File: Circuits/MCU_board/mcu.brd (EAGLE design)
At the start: 100 x 80 mm, 40 parts, among them IC1 RP111N331B-TR-FE, U1 TCA9548APWR, U2 USBLC6-2P6, U4 LSM9DS1, U5 STM32L452RECT6

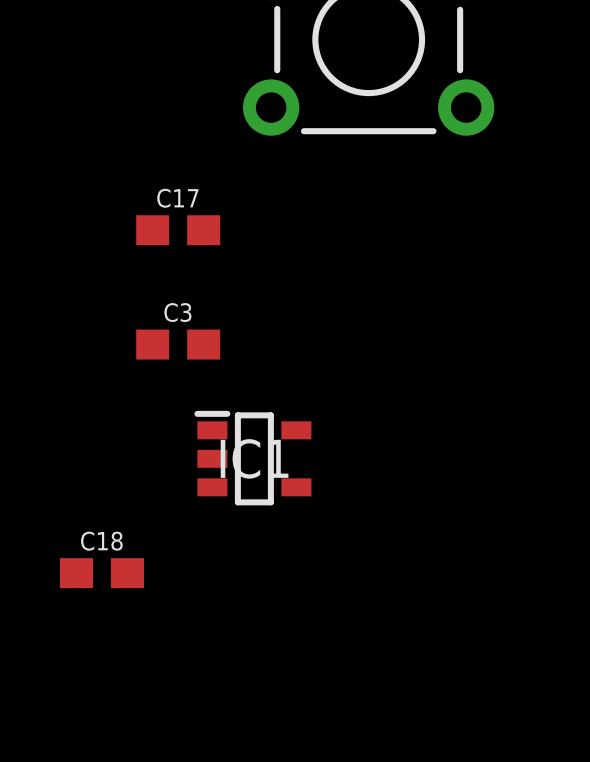
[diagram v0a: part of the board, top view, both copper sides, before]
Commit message: Changed all VCC to VDD, Fixed i2c bus issue for board IMU and baseboard IMU
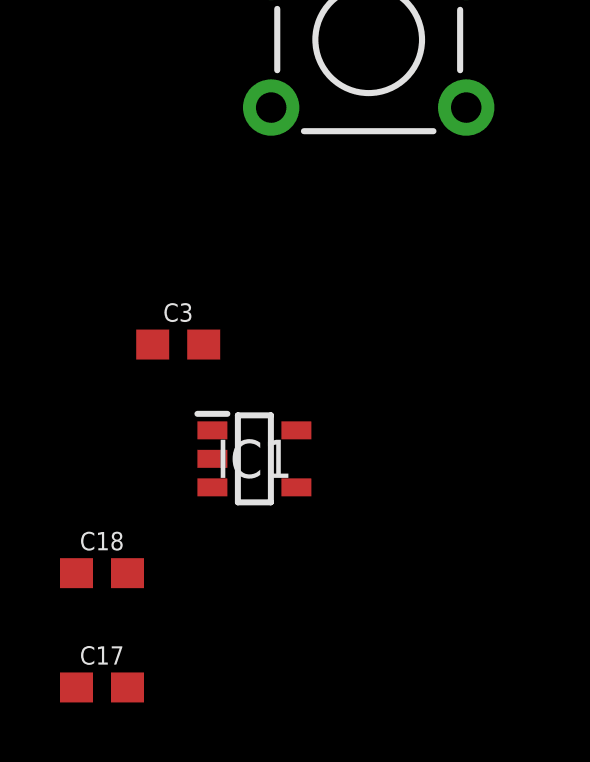
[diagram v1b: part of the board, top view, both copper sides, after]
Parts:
- C17: value 100nF -> 0.1uF
- moved C17 15.5 mm to (-50.8, -138.4)
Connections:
- removed net VCC: C2.1, C6.1, C8.1, R1.2, R2.2, R3.2, R4.2, R6.2, U4.1, U4.22, U4.23, U4.3
- net SCL5: no longer U$5.5
- net SCL6: no longer U4.2
- net SCL7: now also U$5.5, U4.2
- net SDA5: no longer U$5.6
- net SDA6: no longer U4.4
- net SDA7: now also U$5.6, U4.4
- net VDD: now also C2.1, C6.1, C8.1, R1.2, R2.2, R3.2, R4.2, R6.2, U4.1, U4.22, U4.23, U4.3
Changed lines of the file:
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@@
 <attribute name="VALUE" x="-41.91" y="-120.015" size="0.6096" layer="27" font="vector" ratio="20" align="top-center"/>
-</element>
-<element name="C17" library="SparkFun-Capacitors" package="0603" value="100nF" x="-48.26" y="-123.19" smashed="yes">
-<attribute name="NAME" x="-48.26" y="-122.428" size="0.6096" layer="25" font="vector" ratio="20" align="bottom-center"/>
-<attribute name="PROD_ID" value="CAP-12380" x="-48.26" y="-123.19" size="1.778" layer="27" display="off"/>
-<attribute name="VALUE" x="-48.26" y="-123.952" size="0.6096" layer="27" font="vector" ratio="20" align="top-center"/>
 </element>
 <element name="C3" library="SparkFun-Capacitors" package="0603" value="1 uF" x="-48.26" y="-127" smashed="yes">
@@
 <attribute name="VALUE" x="-50.8" y="-135.382" size="0.6096" layer="27" font="vector" ratio="20" align="top-center"/>
 </element>
+<element name="C17" library="SparkFun-Capacitors" package="0603" value="0.1uF" x="-50.8" y="-138.43" smashed="yes">
+<attribute name="NAME" x="-50.8" y="-137.668" size="0.6096" layer="25" font="vector" ratio="20" align="bottom-center"/>
+<attribute name="PROD_ID" value="CAP-00810" x="-50.8" y="-138.43" size="1.778" layer="27" display="off"/>
+<attribute name="VALUE" x="-50.8" y="-139.192" size="0.6096" layer="27" font="vector" ratio="20" align="top-center"/>
+</element>
 </elements>
 <signals>
 <signal name="VBAT">
 <contactref element="U5" pad="1"/>
-</signal>
-<signal name="VCC">
-<contactref element="U4" pad="23"/>
-<contactref element="U4" pad="22"/>
-<contactref element="C6" pad="1"/>
-<contactref element="C8" pad="1"/>
-<contactref element="U4" pad="1"/>
-<contactref element="U4" pad="3"/>
-<contactref element="C2" pad="1"/>
-<contactref element="R4" pad="2"/>
-<contactref element="R3" pad="2"/>
-<contactref element="R2" pad="2"/>
-<contactref element="R1" pad="2"/>
-<contactref element="R6" pad="2"/>
-<wire x1="-43.6" y1="-16.51" x2="-43.6" y2="-110.49" width="0" layer="19" extent="1-1"/>
-<wire x1="-43.6" y1="-12.7" x2="-43.6" y2="-16.51" width="0" layer="19" extent="1-1"/>
-<wire x1="-39.79" y1="-12.7" x2="-43.6" y2="-12.7" width="0" layer="19" extent="1-1"/>
-<wire x1="-35.98" y1="-12.7" x2="-39.79" y2="-12.7" width="0" layer="19" extent="1-1"/>
-<wire x1="-45.3" y1="-8.89" x2="-43.6" y2="-12.7" width="0" layer="19" extent="1-1"/>
-<wire x1="-37.68" y1="-8.89" x2="-35.98" y2="-12.7" width="0" layer="19" extent="1-1"/>
-<wire x1="-45.925" y1="-3.595" x2="-45.3" y2="-8.89" width="0" layer="19" extent="1-1"/>
-<wire x1="-45.955" y1="-2.585" x2="-45.925" y2="-3.595" width="0" layer="19" extent="1-1"/>
-<wire x1="-45.095" y1="-2.585" x2="-45.955" y2="-2.585" width="0" layer="19" extent="1-1"/>
-<wire x1="-44.665" y1="-2.585" x2="-45.095" y2="-2.585" width="0" layer="19" extent="1-1"/>
-<wire x1="-37.68" y1="-2.54" x2="-37.68" y2="-8.89" width="0" layer="19" extent="1-1"/>
 </signal>
 <signal name="GND">
@@
 <contactref element="R5" pad="1"/>
 <contactref element="S1" pad="1"/>
-<contactref element="C17" pad="2"/>
 <contactref element="C3" pad="2"/>
 <contactref element="C5" pad="2"/>
@@
 <contactref element="U2" pad="2"/>
 <contactref element="C18" pad="2"/>
+<contactref element="C17" pad="2"/>
+<wire x1="-49.95" y1="-134.62" x2="-49.95" y2="-138.43" width="0" layer="19" extent="1-1"/>
 <wire x1="-47.12" y1="-130.81" x2="-49.95" y2="-134.62" width="0" layer="19" extent="1-1"/>
 <wire x1="-47.41" y1="-127" x2="-47.12" y2="-130.81" width="0" layer="19" extent="1-1"/>
-<wire x1="-47.41" y1="-123.19" x2="-47.41" y2="-127" width="0" layer="19" extent="1-1"/>
-<wire x1="-45.1612" y1="-114.5794" x2="-47.41" y2="-123.19" width="0" layer="19" extent="1-1"/>
+<wire x1="-45.1612" y1="-114.5794" x2="-47.41" y2="-127" width="0" layer="19" extent="1-1"/>
 <wire x1="-45.3" y1="-106.68" x2="-45.1612" y2="-114.5794" width="0" layer="19" extent="1-1"/>
 <wire x1="-44.45" y1="-102.87" x2="-45.3" y2="-106.68" width="0" layer="19" extent="1-1"/>
@@
 <contactref element="IC1" pad="5"/>
 <contactref element="IC1" pad="4"/>
+<contactref element="R6" pad="2"/>
+<contactref element="U4" pad="23"/>
+<contactref element="U4" pad="22"/>
+<contactref element="C6" pad="1"/>
+<contactref element="C8" pad="1"/>
+<contactref element="U4" pad="1"/>
+<contactref element="U4" pad="3"/>
+<contactref element="C2" pad="1"/>
+<contactref element="R1" pad="2"/>
+<contactref element="R2" pad="2"/>
+<contactref element="R3" pad="2"/>
+<contactref element="R4" pad="2"/>
 <wire x1="-44.32" y1="-129.86" x2="-49.11" y2="-127" width="0" layer="19" extent="1-1"/>
 <wire x1="-44.32" y1="-131.76" x2="-44.32" y2="-129.86" width="0" layer="19" extent="1-1"/>
-<wire x1="-44.45" y1="-97.79" x2="-49.11" y2="-127" width="0" layer="19" extent="1-1"/>
+<wire x1="-43.6" y1="-110.49" x2="-49.11" y2="-127" width="0" layer="19" extent="1-1"/>
+<wire x1="-44.45" y1="-97.79" x2="-43.6" y2="-110.49" width="0" layer="19" extent="1-1"/>
 <wire x1="-38.91" y1="-80.08" x2="-44.45" y2="-97.79" width="0" layer="19" extent="1-1"/>
 <wire x1="-38.91" y1="-71.19" x2="-38.91" y2="-80.08" width="0" layer="19" extent="1-1"/>
@@
 <wire x1="-45.3" y1="-24.13" x2="-45.3" y2="-27.94" width="0" layer="19" extent="1-1"/>
 <wire x1="-45.3" y1="-20.32" x2="-45.3" y2="-24.13" width="0" layer="19" extent="1-1"/>
-<wire x1="-23.07" y1="1.87" x2="-45.3" y2="-20.32" width="0" layer="19" extent="1-1"/>
+<wire x1="-43.6" y1="-16.51" x2="-45.3" y2="-20.32" width="0" layer="19" extent="1-1"/>
+<wire x1="-43.6" y1="-12.7" x2="-43.6" y2="-16.51" width="0" layer="19" extent="1-1"/>
+<wire x1="-39.79" y1="-12.7" x2="-43.6" y2="-12.7" width="0" layer="19" extent="1-1"/>
+<wire x1="-35.98" y1="-12.7" x2="-39.79" y2="-12.7" width="0" layer="19" extent="1-1"/>
+<wire x1="-45.3" y1="-8.89" x2="-43.6" y2="-12.7" width="0" layer="19" extent="1-1"/>
+<wire x1="-37.68" y1="-8.89" x2="-35.98" y2="-12.7" width="0" layer="19" extent="1-1"/>
+<wire x1="-45.925" y1="-3.595" x2="-45.3" y2="-8.89" width="0" layer="19" extent="1-1"/>
+<wire x1="-45.955" y1="-2.585" x2="-45.925" y2="-3.595" width="0" layer="19" extent="1-1"/>
+<wire x1="-45.095" y1="-2.585" x2="-45.955" y2="-2.585" width="0" layer="19" extent="1-1"/>
+<wire x1="-44.665" y1="-2.585" x2="-45.095" y2="-2.585" width="0" layer="19" extent="1-1"/>
+<wire x1="-37.68" y1="-2.54" x2="-37.68" y2="-8.89" width="0" layer="19" extent="1-1"/>
+<wire x1="-23.07" y1="1.87" x2="-37.68" y2="-2.54" width="0" layer="19" extent="1-1"/>
 <wire x1="-16.57" y1="1.87" x2="-23.07" y2="1.87" width="0" layer="19" extent="1-1"/>
 <wire x1="-14.57" y1="11.37" x2="-16.57" y2="1.87" width="0" layer="19" extent="1-1"/>
@@
 <signal name="SCL7">
 <contactref element="U1" pad="20"/>
+<contactref element="U$5" pad="5"/>
+<contactref element="U4" pad="2"/>
+<wire x1="-45.925" y1="-3.165" x2="-37.91" y2="-80.08" width="0" layer="19" extent="1-1"/>
+<wire x1="34.585" y1="57.5278" x2="-45.925" y2="-3.165" width="0" layer="19" extent="1-1"/>
 </signal>
 <signal name="SDA7">
 <contactref element="U1" pad="19"/>
+<contactref element="U$5" pad="6"/>
+<contactref element="U4" pad="4"/>
+<wire x1="-45.925" y1="-4.025" x2="-36.91" y2="-80.08" width="0" layer="19" extent="1-1"/>
+<wire x1="35.235" y1="57.5278" x2="-45.925" y2="-4.025" width="0" layer="19" extent="1-1"/>
 </signal>
 <signal name="SCL6">
 <contactref element="U1" pad="18"/>
 <contactref element="U$5" pad="1"/>
-<contactref element="U4" pad="2"/>
-<wire x1="-45.925" y1="-3.165" x2="-41.91" y2="-80.08" width="0" layer="19" extent="1-1"/>
-<wire x1="35.885" y1="57.5278" x2="-45.925" y2="-3.165" width="0" layer="19" extent="1-1"/>
+<wire x1="35.885" y1="57.5278" x2="-41.91" y2="-80.08" width="0" layer="19" extent="1-1"/>
 </signal>
 <signal name="SDA6">
 <contactref element="U1" pad="17"/>
 <contactref element="U$5" pad="2"/>
-<contactref element="U4" pad="4"/>
-<wire x1="-45.925" y1="-4.025" x2="-40.91" y2="-80.08" width="0" layer="19" extent="1-1"/>
-<wire x1="36.535" y1="57.5278" x2="-45.925" y2="-4.025" width="0" layer="19" extent="1-1"/>
+<wire x1="36.535" y1="57.5278" x2="-40.91" y2="-80.08" width="0" layer="19" extent="1-1"/>
 </signal>
 <signal name="SCL5">
 <contactref element="U1" pad="16"/>
 <contactref element="U$4" pad="1"/>
-<contactref element="U$5" pad="5"/>
-<wire x1="-41.91" y1="-71.19" x2="-37.91" y2="-80.08" width="0" layer="19" extent="1-1"/>
 <wire x1="37.185" y1="57.5278" x2="-41.91" y2="-71.19" width="0" layer="19" extent="1-1"/>
 </signal>
@@
 <contactref element="U1" pad="15"/>
 <contactref element="U$4" pad="2"/>
-<contactref element="U$5" pad="6"/>
-<wire x1="-40.91" y1="-71.19" x2="-36.91" y2="-80.08" width="0" layer="19" extent="1-1"/>
 <wire x1="37.835" y1="57.5278" x2="-40.91" y2="-71.19" width="0" layer="19" extent="1-1"/>
 </signal>
@@
 <signal name="N$4">
 <contactref element="S1" pad="3"/>
+<contactref element="U5" pad="7"/>
 <contactref element="C17" pad="1"/>
-<contactref element="U5" pad="7"/>
-<wire x1="-45.1612" y1="-119.1006" x2="-49.11" y2="-123.19" width="0" layer="19" extent="1-1"/>
+<wire x1="-45.1612" y1="-119.1006" x2="-51.65" y2="-138.43" width="0" layer="19" extent="1-1"/>
 <wire x1="-26.07" y1="8.37" x2="-45.1612" y2="-119.1006" width="0" layer="19" extent="1-1"/>
 </signal>

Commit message: Added i2c resistors - pulled high, Fixed capacitor package size, moved schematics around to be more organized
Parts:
- added R10, R11, R12, R13, R14, R15, R16, R17, R18, R19, R20, R7, R8, R9: 4.7k, SparkFun-Resistors:0603
- C11, C13, C15, C9: value 100nF -> 0.1uF
- C3: value 1 uF -> 1.0uF
- C5: device SparkFun-Capacitors:0402 -> SparkFun-Capacitors:0603
- R1, R3: value 10k -> 4.7k
- moved C5 320.2 mm to (-50.8, -276.9)
- moved C10 283.3 mm to (-50.8, -307.3)
- moved C12 279.5 mm to (-50.8, -311.1)
- moved C14 275.7 mm to (-50.8, -315.0)
- moved C9 271.9 mm to (-50.8, -292.1)
- moved C16 271.9 mm to (-50.8, -318.8)
- moved C11 268.0 mm to (-50.8, -295.9)
- moved C13 264.2 mm to (-50.8, -299.7)
- moved C15 260.4 mm to (-50.8, -303.5)
- moved R3 192.3 mm to (-50.8, -204.5)
- moved R1 188.1 mm to (-50.8, -200.7)
- moved R4 161.0 mm to (-0.85, -171.4)
- moved C3 153.7 mm to (-50.8, -280.7)
- moved R2 151.4 mm to (-0.85, -158.8)
- moved C17 123.2 mm to (-50.8, -261.6)
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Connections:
- removed net SA0: R1.1, U4.5
- removed net SA1: R3.1, U4.6
- new net N$3: C17.1
- net GND: now also U4.5, U4.6
- net N$4: no longer C17.1
- net SCL0: now also R3.1
- net SCL1: now also R8.1
- net SCL2: now also R10.1
- net SCL3: now also R12.1
- net SCL4: now also R14.1
- net SCL5: now also R16.1
- net SCL6: now also R18.1
- net SCL7: now also R20.1
- net SDA0: now also R1.1
- net SDA1: now also R7.1
- net SDA2: now also R9.1
- net SDA3: now also R11.1
- net SDA4: now also R13.1
- net SDA5: now also R15.1
- net SDA6: now also R17.1
- net SDA7: now also R19.1
- net VDD: now also R10.2, R11.2, R12.2, R13.2, R14.2, R15.2, R16.2, R17.2, R18.2, R19.2, R20.2, R7.2, R8.2, R9.2

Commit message: Add FTDI chip to MCU board
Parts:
- added C19: 4.7uF, SparkFun-Capacitors:0603
- added C20, C21: 0.1uF, SparkFun-Capacitors:0603
- added C22: 10nF, SparkFun-Capacitors:0603
- added C23, C24: 47pF, SparkFun-Capacitors:0603
- added IC2: FT230XS, ftdichip:SSOP16
- added MI0603K300R-10: 30Ω/1.8A, SparkFun-Coils:0603
- added R21, R22, R27, R28: 4.7k, SparkFun-Resistors:0603
- added R23, R24, R25, R26: 10k, SparkFun-Resistors:0603
- added RX_LED, TX_LED: GREEN, SparkFun-LED:LED-0603
- moved R20 398.1 mm to (-0.85, -652.8)
- moved R19 389.3 mm to (-0.85, -640.1)
- moved R18 380.5 mm to (-0.85, -627.4)
- moved R17 371.7 mm to (-0.85, -614.7)
- moved R16 362.9 mm to (-0.85, -602.0)
- moved R15 354.1 mm to (-0.85, -589.3)
- moved R14 345.3 mm to (-0.85, -576.6)
- moved R13 336.5 mm to (-0.85, -563.9)
- moved R12 327.7 mm to (-0.85, -551.2)
- moved R11 318.9 mm to (-0.85, -538.5)
- moved R10 310.1 mm to (-0.85, -525.8)
- moved R9 301.3 mm to (-0.85, -513.1)
- moved R8 292.6 mm to (-0.85, -500.4)
- moved R7 283.8 mm to (-0.85, -487.7)
- moved R3 275.1 mm to (-0.85, -475.0)
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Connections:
- net N$4 renamed NRST
- new net CTS: IC2.6, R25.1, U5.14
- new net N$10: R28.2, RX_LED.A
- new net N$11: IC2.7, RX_LED.C
- new net N$6: IC2.9, R21.2
- new net N$7: IC2.8, R22.1
- new net N$8: R27.2, TX_LED.A
- new net N$9: IC2.14, TX_LED.C
- new net RTS: IC2.2, R26.1, U5.15
- new net RXD: IC2.4, R24.1, U5.17
- new net TXD: IC2.1, R23.1, U5.16
- new net VCCIO: C20.1, IC2.10, IC2.11, IC2.3, R23.2, R24.2, R25.2, R26.2
- new net VCC_USB: C19.1, C21.1, IC2.12, MI0603K300R-10.1
- net GND: now also C19.2, C20.2, C21.2, C22.2, C23.2, C24.2, IC2.13, IC2.5
- net USB_D+: now also C24.1, R22.2
- net USB_D-: now also C23.1, R21.1
- net VBUS: now also C22.1, MI0603K300R-10.2
- net VDD: now also R27.1, R28.1

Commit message: Fix resistors in FTDI
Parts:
- R21, R22: value 4.7k -> 27R
- R27, R28: value 4.7k -> 270R
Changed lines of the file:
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@@
 <attribute name="VALUE" x="-50.8" y="-334.772" size="0.6096" layer="27" font="vector" ratio="20" align="top-center"/>
 </element>
-<element name="R21" library="SparkFun-Resistors" package="0603" value="4.7k" x="-0.85" y="-665.48" smashed="yes">
+<element name="R21" library="SparkFun-Resistors" package="0603" value="27R" x="-0.85" y="-665.48" smashed="yes">
 <attribute name="NAME" x="-0.85" y="-664.718" size="0.6096" layer="25" font="vector" ratio="20" align="bottom-center"/>
 <attribute name="PROD_ID" value="RES-07857" x="-0.85" y="-665.48" size="1.778" layer="27" display="off"/>
 <attribute name="VALUE" x="-0.85" y="-666.242" size="0.6096" layer="27" font="vector" ratio="20" align="top-center"/>
 </element>
-<element name="R22" library="SparkFun-Resistors" package="0603" value="4.7k" x="-0.85" y="-678.18" smashed="yes">
+<element name="R22" library="SparkFun-Resistors" package="0603" value="27R" x="-0.85" y="-678.18" smashed="yes">
 <attribute name="NAME" x="-0.85" y="-677.418" size="0.6096" layer="25" font="vector" ratio="20" align="bottom-center"/>
 <attribute name="PROD_ID" value="RES-07857" x="-0.85" y="-678.18" size="1.778" layer="27" display="off"/>
@@
 <attribute name="VALUE" x="-52.07" y="-365.252" size="0.6096" layer="27" font="vector" ratio="20" align="top-center"/>
 </element>
-<element name="R27" library="SparkFun-Resistors" package="0603" value="4.7k" x="-0.85" y="-690.88" smashed="yes">
+<element name="R27" library="SparkFun-Resistors" package="0603" value="270R" x="-0.85" y="-690.88" smashed="yes">
 <attribute name="NAME" x="-0.85" y="-690.118" size="0.6096" layer="25" font="vector" ratio="20" align="bottom-center"/>
 <attribute name="PROD_ID" value="RES-07857" x="-0.85" y="-690.88" size="1.778" layer="27" display="off"/>
@@
 <attribute name="VALUE" x="-52.07" y="-399.415" size="0.6096" layer="27" font="vector" ratio="20" align="top-center"/>
 </element>
-<element name="R28" library="SparkFun-Resistors" package="0603" value="4.7k" x="-0.85" y="-703.58" smashed="yes">
+<element name="R28" library="SparkFun-Resistors" package="0603" value="270R" x="-0.85" y="-703.58" smashed="yes">
 <attribute name="NAME" x="-0.85" y="-702.818" size="0.6096" layer="25" font="vector" ratio="20" align="bottom-center"/>
 <attribute name="PROD_ID" value="RES-07857" x="-0.85" y="-707.39" size="1.778" layer="27" display="off"/>

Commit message: Moved and grouped all components into board area, measured maximum board area
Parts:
- moved R23 734.4 mm to (32.0, 23.5)
- moved R24 734.4 mm to (32.0, 20.9)
- moved R25 734.4 mm to (32.0, 18.4)
- moved R26 734.4 mm to (32.0, 15.9)
- moved R28 719.7 mm to (43.9, 14.7)
- moved R27 710.4 mm to (43.6, 18.1)
- moved R22 701.3 mm to (43.9, 21.7)
- moved R20 696.6 mm to (66.2, 40.6), turned to 180 degrees
- moved R21 691.7 mm to (43.8, 24.8)
- moved R19 686.9 mm to (66.2, 43.5), turned to 180 degrees
- moved R16 676.6 mm to (78.3, 69.9), turned to 270 degrees
- moved R18 665.5 mm to (66.2, 34.7), turned to 180 degrees
- moved R15 663.7 mm to (75.8, 70.0), turned to 270 degrees
- moved R17 655.4 mm to (66.2, 37.3), turned to 180 degrees
- moved R14 650.5 mm to (64.0, 70.7), turned to 270 degrees
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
